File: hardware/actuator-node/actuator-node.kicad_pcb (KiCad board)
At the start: 2 copper layers, 50 x 45 mm, 57 parts, among them J1 PHASES, J2 CAN IN, J3 CAN EXT, J4 19V IN, J5 SWD, J6 ENCODER, J7 NTC, M1 SimpleFOC Mini, U1 STM32G431CBT6, U2 SN65HVD230, U4 INA240A1D, U5 INA240A1D, U6 AMS1117-3.3, Y1 8 MHz

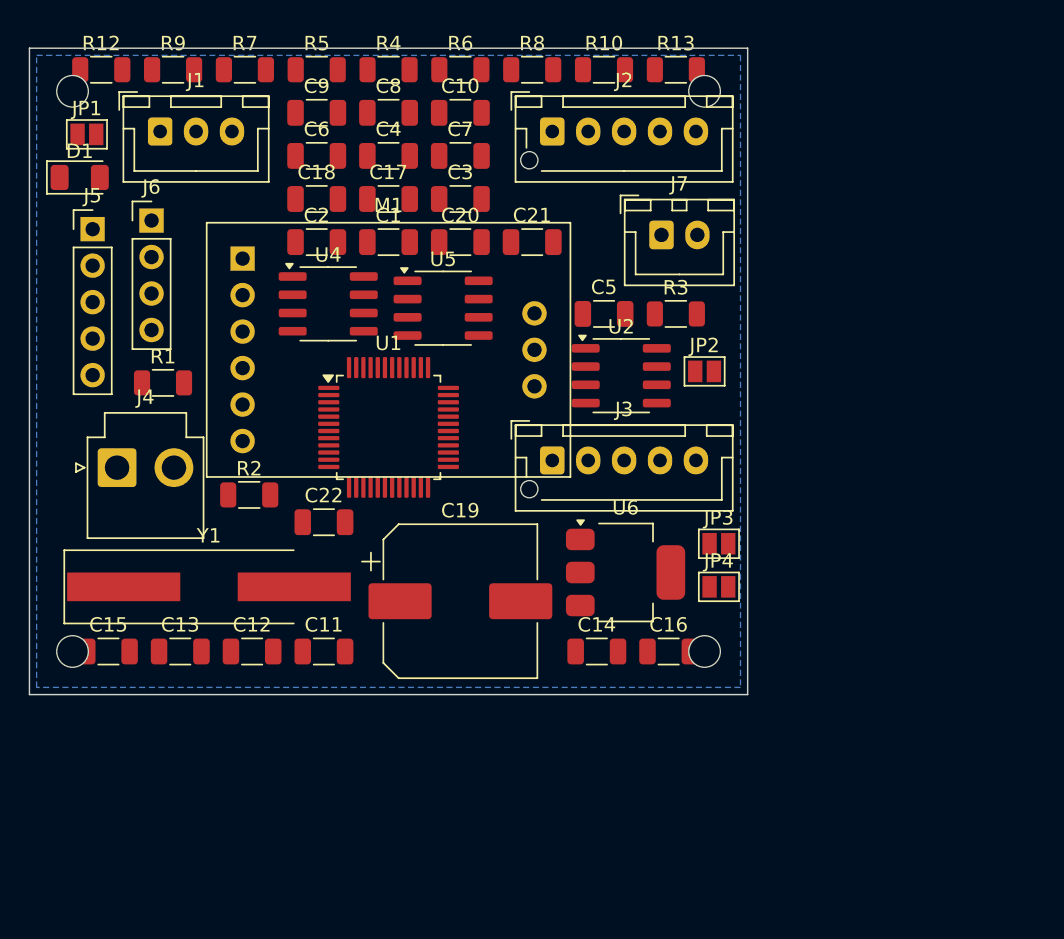
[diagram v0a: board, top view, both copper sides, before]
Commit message: Rebuild both boards from the real driver module, grouped by function
The vendor's EasyEDA export of the driver module arrived, so its footprint is
now measured rather than guessed: 17 pins and four mounting holes over
22.6 x 18.2 mm, read from vendor/simplefoc_stepmini.json at build time.

The export also settles three things that were open, and raises one:

- The module's 3V3 pin is a supply input. Its nSLEEP and nRESET pull-ups hang
  off it and there is no regulator on the board, so leaving it open would have
  left the driver possibly held in reset. It is now wired to the 3.3 V rail.
- The header's enable pin sits behind a series resistor into the driver's EN,
  so the kill line drives it directly and nSLEEP/nRESET need no connection.
- nFAULT is brought out with its own pull-up, so it now goes to PB4.
- The export shows a quad half-bridge - IN1-IN4 and OUT1-OUT4 - not the
  three-in/three-out DRV8313 the build console names. A 3-phase motor uses
  three of the four channels, so it works, but it is not the specified part.
  Flagged in the actuator README rather than silently accepted.

Placement is now by functional block. Each block keeps its own passives, and
parts with an electrical reason to hug another are placed against it and
checked: the crystal is held within 12 mm of the MCU and its load caps within
9 mm of it, which the previous layout failed at 32 mm. Microphone spacing is
pinned at exactly 130 mm and verified. Both boards are larger - the node goes
to 70 x 60 and the base to 170 x 100 - which is what buys room to group and
still route by hand.

Indicators added on both boards, using the XL-3216SURC red 1206 that is on
hand. Series resistors are sized for its 2.4 V forward drop rather than left at
a default: 220 R on 3.3 V rails, 470 R on the 5 V one.

check.py grew to match: it now verifies group membership, pinned positions and
proximity constraints alongside the netlist, and each project carries a
colour-coded placement.svg.

Co-Authored-By: Claud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
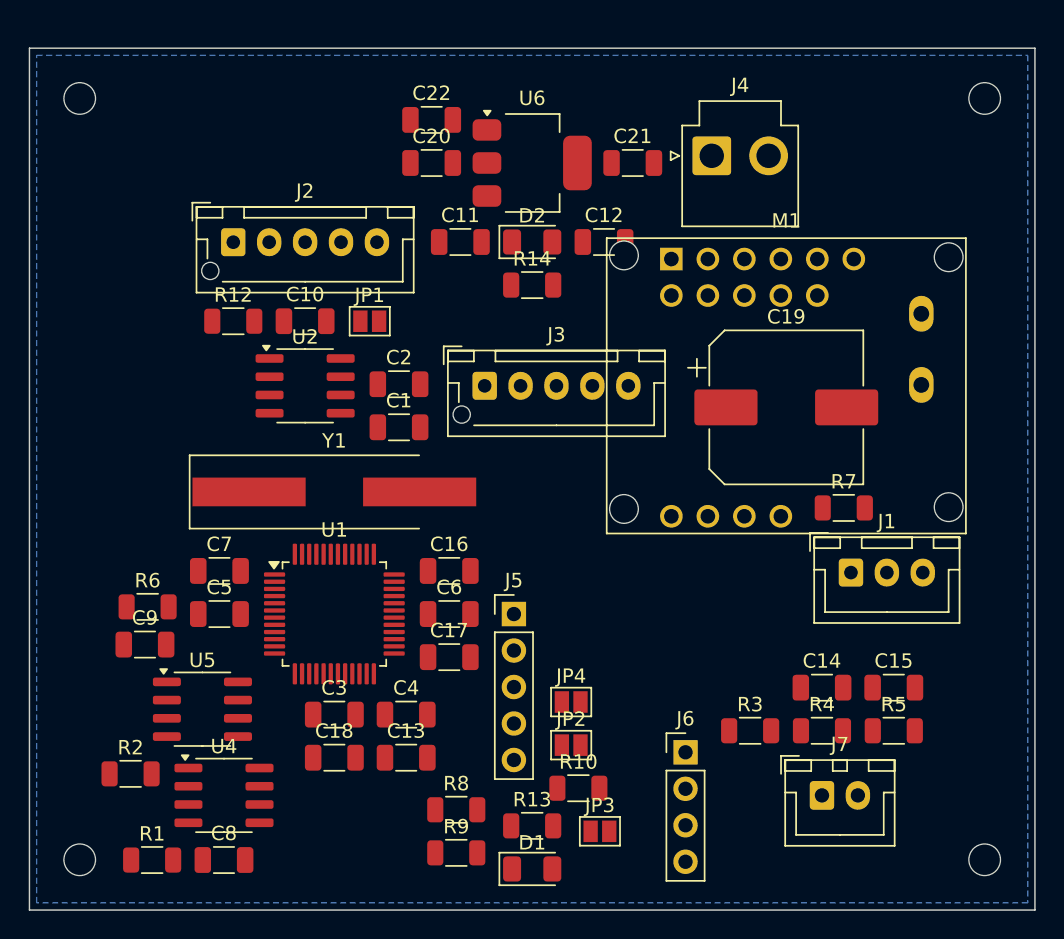
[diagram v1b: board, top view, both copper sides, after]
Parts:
- added D2: XL-3216SURC red, LED_SMD:LED_1206_3216Metric, F.Cu at (35.0, 13.5)
- added R14: 220R, Resistor_SMD:R_1206_3216Metric, F.Cu at (35.0, 16.5)
- D1: value red -> XL-3216SURC red
- R13: value 120R -> 220R
- moved R5 61.1 mm to (60.2, 47.5)
- moved R9 58.0 mm to (29.7, 56.0)
- moved D1 57.5 mm to (35.0, 57.1)
- moved J1 57.1 mm to (57.2, 36.5)
- moved R4 55.0 mm to (55.2, 47.5)
- moved C15 54.7 mm to (60.2, 44.5)
- moved R13 53.6 mm to (35.0, 54.1)
- moved C8 53.3 mm to (13.5, 56.5)
- moved J6 52.5 mm to (45.7, 49.0)
- moved R8 51.8 mm to (29.7, 53.0)
- moved R7 51.7 mm to (56.7, 32.0)
- moved R10 50.0 mm to (38.2, 51.5)
- moved J4 46.7 mm to (47.5, 7.49)
- moved R6 43.3 mm to (8.23, 38.9)
- moved J7 40.6 mm to (55.2, 52.0)
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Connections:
- M1 pad 4: DRV_EN -> (no net)
- M1 pad 5: +19V -> DRV_EN
- M1 pad 7: PH_A_DRV -> DRV_nFAULT
- M1 pad 8: PH_B_DRV -> (no net)
- M1 pad 9: PH_C -> (no net)
- U1 pad 41: (no net) -> DRV_nFAULT
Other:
- board size 50 x 45 mm -> 70 x 60 mm
- board text added: "analog"
- board text added: "can"
- board text added: "clock"
- board text added: "drive"
- board text added: "gearbox sits over this circle on the BACK face - keep rear protrusion under 5.5 mm"
- board text added: "isense"
- board text added: "mcu"
- board text added: "nodeid"
- board text added: "power"
- board text added: "status"
- board text removed: "gearbox above - 5.5 mm ceiling inside this circle"

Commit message: Rebuild the driver module around the real SimpleFOC Mini v1.0
The EasyEDA export the footprint was generated from was a different product:
a "step mini" quad half-bridge with IN1-IN4 and four outputs, where the board
on the bench is a SimpleFOC Mini v1.0 (DRV8313, three phases, dated 04/22).
The generated footprint carried phantom IN4/OUT4 pins, the wrong row order and
the wrong geometry, and would not have populated.

Everything now comes from the v1.0 exports. The PCB export gives pad geometry;
the schematic export resolves that PCB's anonymous U1_nn nets to real signals
and is what settled the important question below. Both step-mini exports are
removed.

Fixes a real bug this uncovered. The module's 3V3 header pin is DRV8313 pin 15,
V3P3OUT - an internal regulator output, not a supply input as previously
assumed. It had been wired to the carrier's 3.3 V rail, which would have
connected the AMS1117's output to the module's own regulator. It is now left
open, and check.py fails the build if it reappears on any net. That same
regulator feeds the module's nSlp/nRes/nFlt pull-ups, which is why those three
need no connection to idle in the running state.

The module's reference becomes A1 rather than M1, so its pins can carry the
silkscreen names M1/M2/M3 without ("M1", "M1") appearing in the netlist.

Two generator fixes fell out of the rebuild:

- simplefoc_from_json() now reads pads nested inside LIB entries, because on
  this board the headers are placed as components - only 6 of the 19 pads are
  top-level shapes - while filtering to the HDR-* components so the driver IC's
  own 29 pads stay out.
- Proximity placement follows each chain depth-first and ranks candidates by
  distance to the target's courtyard rather than to its origin. Breadth-first
  ranking by origin put a crystal load cap 3.8 mm clear of a crystal whose
  courtyard is 20 mm wide; both caps now sit inside 2 mm. check.py measures the
  same way, edge to edge, since centre-to-centre was mostly mea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
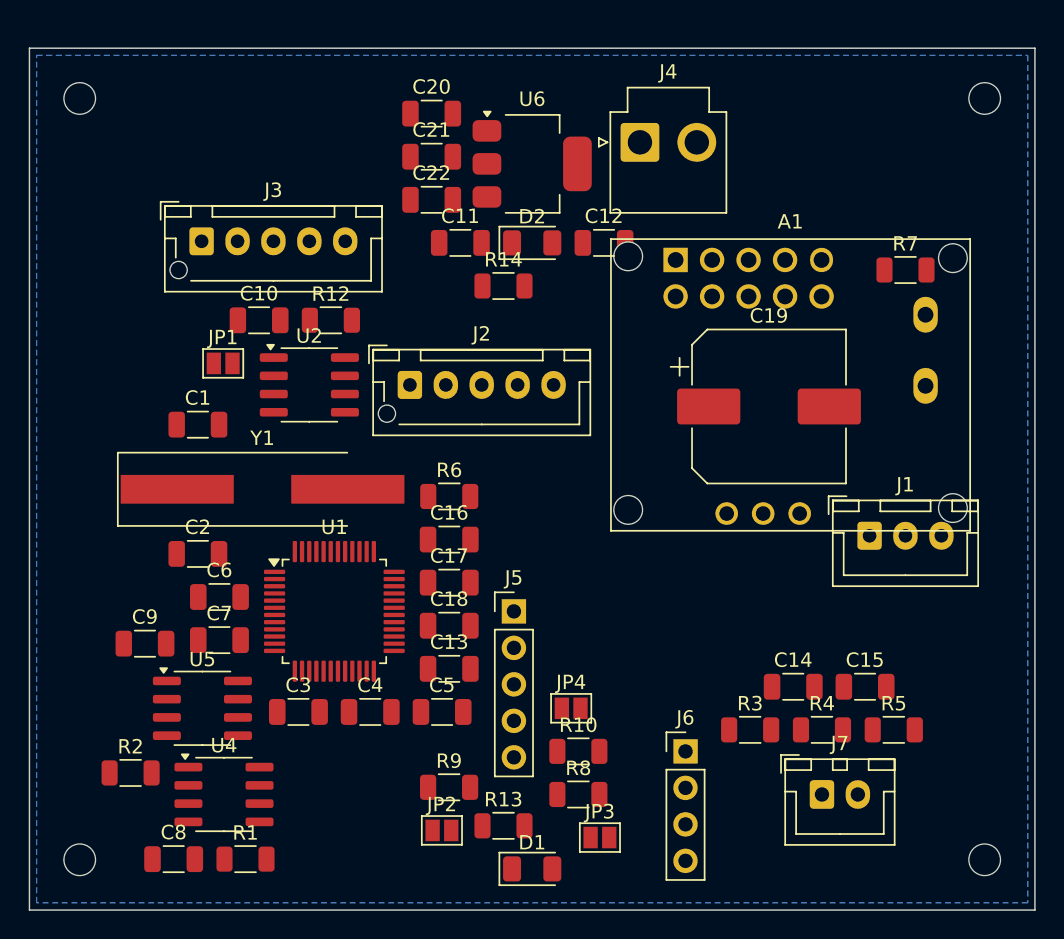
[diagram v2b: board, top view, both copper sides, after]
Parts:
- removed M1: SimpleFOC Mini, juno:SimpleFOC_Mini_Socket
- added A1: SimpleFOC Mini v1.0, juno:SimpleFOC_Mini_Socket, F.Cu at (53.0, 23.4)
- moved R6 22.4 mm to (29.2, 31.2)
- moved J3 22.1 mm to (12.0, 13.4)
- moved C2 18.3 mm to (11.7, 35.2)
- moved R7 17.1 mm to (61.0, 15.4)
- moved C5 16.9 mm to (28.7, 46.2)
- moved C6 16.0 mm to (13.2, 38.2)
- moved J2 15.8 mm to (26.5, 23.4)
- moved C21 14.0 mm to (28.0, 7.55)
- moved C1 14.0 mm to (11.7, 26.2)
- moved C18 12.2 mm to (29.2, 40.2)
- moved JP2 10.8 mm to (28.7, 54.5)
- moved JP1 10.6 mm to (13.5, 21.9)
- moved R8 8.57 mm to (38.2, 52.0)
- moved C13 6.87 mm to (29.2, 43.2)
- moved R12 6.80 mm to (21.0, 18.9)
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
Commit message: Rebuild the BOM around parts on hand, and target Lion Circuits
Every passive and semiconductor in both boards is now a part that is actually
on the shelf, with docs/parts.md recording the reconciliation. Four
substitutions were needed:

- LED series resistors move from 220R/470R, which are not stocked, to 120R on
  the 3.3 V rails (7.5 mA) and 1k on the brain's 5 V rail (2.6 mA, where 120R
  would exceed the LED's 20 mA rating).
- The kill-line gate series resistor moves from 100R to 120R, immaterial here.
- The reverse-polarity FET becomes the AO3481 that is actually on hand; KiCad
  has no symbol for it, so the projects use AO3401A, the same family and the
  same G/S/D pinout.
- The 10 V zener clamping that FET's gate is not stocked, so the gate is
  divided rather than clamped: 100k source-to-gate and 100k gate-to-ground put
  Vgs at about -9.5 V, which enhances the FET hard and stays well inside its
  rating. Two resistors that are stocked, replacing one part that is not.

Two items have no substitute and must be ordered: 30 mR shunts, without which
there is no current sensing, and an N-channel MOSFET for the kill line, since
the AO3481 on hand is P-channel and cannot pull the EN bus down. The kill line
is the one circuit that should not be improvised.

Also notes that the CD43 inductor supplied with the transceivers has no place
in either board, and why the one plausible use - an LC filter on the node's
5 V input - would resonate at about 28 kHz, right on top of the motor PWM.

For fabrication, the boards now carry plot settings that emit Protel-style
gerber extensions, matching the sample set from Lion Circuits, with the X2
attributes off so the output is plain RS-274X. docs/fabrication.md records
their file naming and the design rules used, and is explicit that their
capability page could not be reached from here, so those rules are a
conservative set rather than a reading of their spec sheet.

Co-Authored-By: Claude Opus 5 <noreply@anthropic.com>
Claude-Sess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
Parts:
- R13, R14: value 220R -> 120R
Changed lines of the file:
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@@
 		(aux_axis_origin 0 0)
 		(grid_origin 0 0)
+		(pcbplotparams
+			(layerselection 0x00000000_00000000_55555555_5755f5ff)
+			(plot_on_all_layers_selection 0x00000000_00000000_00000000_00000000)
+			(disableapertmacros no)
+			(usegerberextensions yes)
+			(usegerberattributes no)
+			(usegerberadvancedattributes no)
+			(creategerberjobfile no)
+			(dashed_line_dash_ratio 12.000000)
+			(dashed_line_gap_ratio 3.000000)
+			(svgprecision 4)
+			(plotframeref no)
+			(mode 1)
+			(useauxorigin no)
+			(hpglpennumber 1)
+			(hpglpenspeed 20)
+			(hpglpendiameter 15.000000)
+			(pdf_front_fp_property_popups yes)
+			(pdf_back_fp_property_popups yes)
+			(dxfpolygonmode yes)
+			(dxfimperialunits yes)
+			(dxfusepcbnewfont yes)
+			(psnegative no)
+			(psa4output no)
+			(plotreference yes)
+			(plotvalue yes)
+			(plotfptext yes)
+			(plotinvisibletext no)
+			(sketchpadsonfab no)
+			(subtractmaskfromsilk no)
+			(outputformat 1)
+			(mirror no)
+			(drillshape 0)
+			(scaleselection 1)
+			(outputdirectory "gerbers/")
+		)
 	)
 	(net 0 "")
@@
 			)
 		)
-		(property "Value" "220R"
+		(property "Value" "120R"
 			(at 0 1.82 0)
 			(layer "F.Fab")
@@
 			)
 		)
-		(property "Value" "220R"
+		(property "Value" "120R"
 			(at 0 1.82 0)
 			(layer "F.Fab")

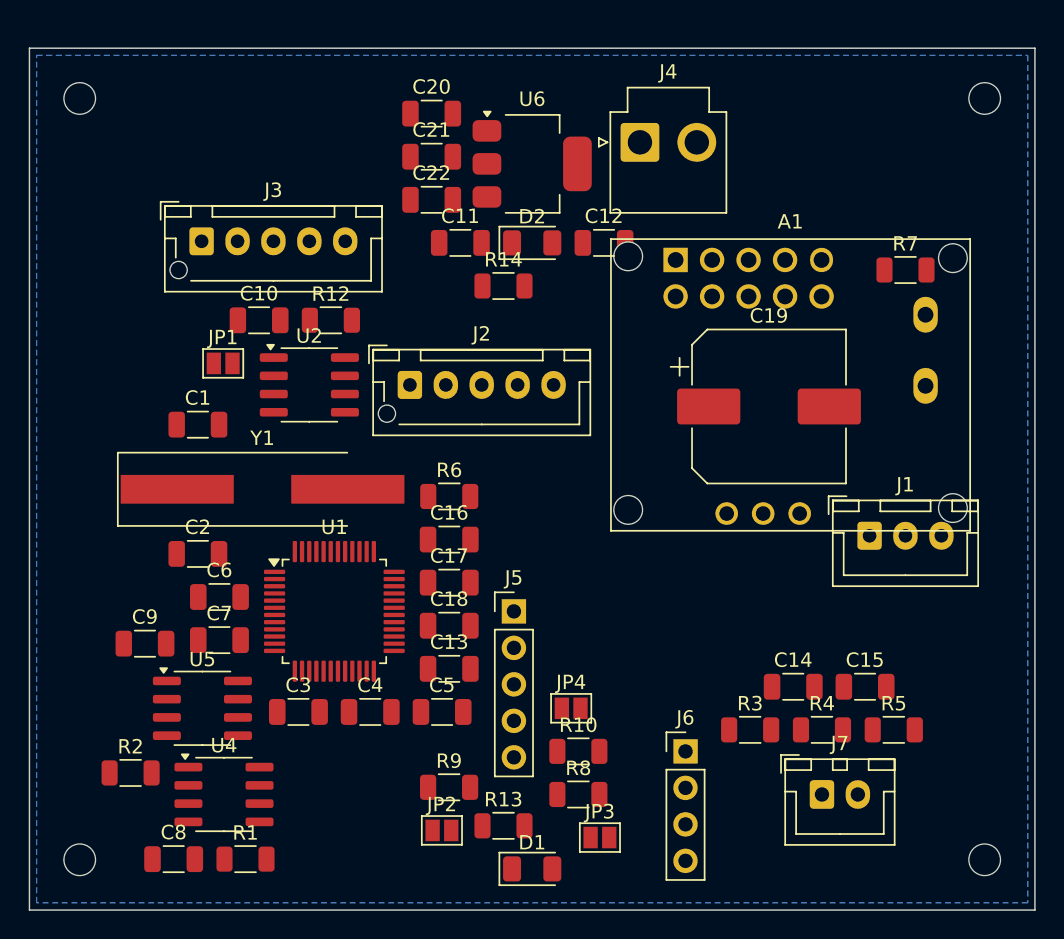
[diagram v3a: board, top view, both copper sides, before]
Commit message: Add an SPI header, floorplan the node, and render assembly views
SPI1 is added as J8, a 1x6 header carrying 3V3, GND, SCK, MISO, MOSI and CS on
PA4-PA7. Those four pins were entirely unused, so an upgrade to an SPI encoder
(AS5047P, MA730, TLE5012B) or an SPI-configured driver costs a header and no
re-assignment. SPI2 would have collided with the driver EN and the node-ID
jumpers, SPI3 with the driver fault line.

Connectors are now pinned to the perimeter on three rules: the two CAN
connectors face each other on opposite edges, since they are a daisy chain;
everything running to the motor - phases, encoder, stator thermistor and the
SPI header - leaves together on one edge as a single loom; and nothing sits in
the interior.

That squeezed the middle enough that auto-placement put the crystal 15 mm from
the MCU and a shunt 16 mm from its amplifier, so the parts that decide the
floorplan are placed by hand: driver socket and its bulk cap, MCU, crystal, and
each shunt beside its own INA240. The Kelvin tap has to land on the shunt's end
caps - at 30 mOhm, 20 mm of copper is a five percent error.

tools/render.py draws the board to SVG from the .kicad_pcb, with no new
dependencies: top assembly with dimensions, mirrored bottom, copper, and a
detail on the driver and MCU. It draws whatever copper is in the file, so the
same views show traces once the board is routed - today it reports zero and
says so on the copper view rather than looking merely empty.

Co-Authored-By: Claude Opus 5 <noreply@anthropic.com>
Claude-Session: https://claude.ai/code/session_011qFNDvbo1RnNn3sy9mr9bh
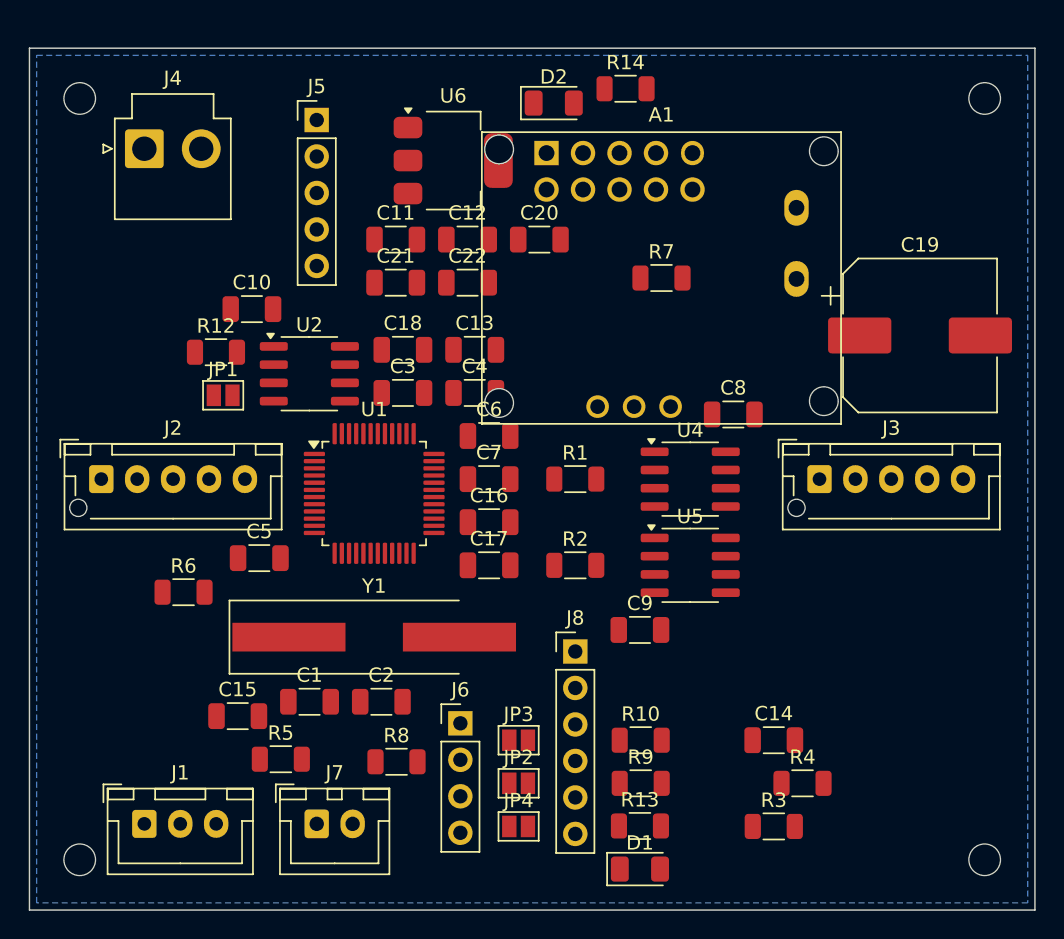
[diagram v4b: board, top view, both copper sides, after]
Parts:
- added J8: SPI, Connector_PinHeader_2.54mm:PinHeader_1x06_P2.54mm_Vertical, F.Cu at (38.0, 42.0)
- moved J1 54.3 mm to (8.00, 54.0)
- moved C8 49.8 mm to (49.0, 25.5)
- moved J3 46.1 mm to (55.0, 30.0)
- moved C15 43.7 mm to (14.5, 46.5)
- moved R5 42.7 mm to (17.5, 49.5)
- moved U4 39.2 mm to (46.0, 30.0)
- moved J5 36.9 mm to (20.0, 5.00)
- moved U5 35.4 mm to (46.0, 36.0)
- moved J7 35.2 mm to (20.0, 54.0)
- moved R1 35.0 mm to (38.0, 30.0)
- moved J4 34.5 mm to (8.00, 7.00)
- moved C9 34.5 mm to (42.5, 40.5)
- moved R2 34.2 mm to (38.0, 36.0)
- moved C3 23.4 mm to (26.0, 24.0)
- moved C4 23.4 mm to (31.0, 24.0)
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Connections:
- U1 pad 12: (no net) -> SPI_CS
- U1 pad 13: (no net) -> SPI_SCK
- U1 pad 14: (no net) -> SPI_MISO
- U1 pad 15: (no net) -> SPI_MOSI
